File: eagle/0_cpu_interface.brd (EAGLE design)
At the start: 160 x 100 mm, 66 parts, among them IC1 74LS08N, IC10 74LS74N, IC11 74LS73N, IC12 MAX1232CPA, IC13 74LS32N, IC14 74LS244N, IC15 74LS74N, IC16 74LS14N, IC17 74LS541N, IC18 74LS541N, IC19 74LS541N, IC2 74LS541N, IC3 74LS245N, IC4 74LS245N, IC6 74LS541N, IC9 74LS74N

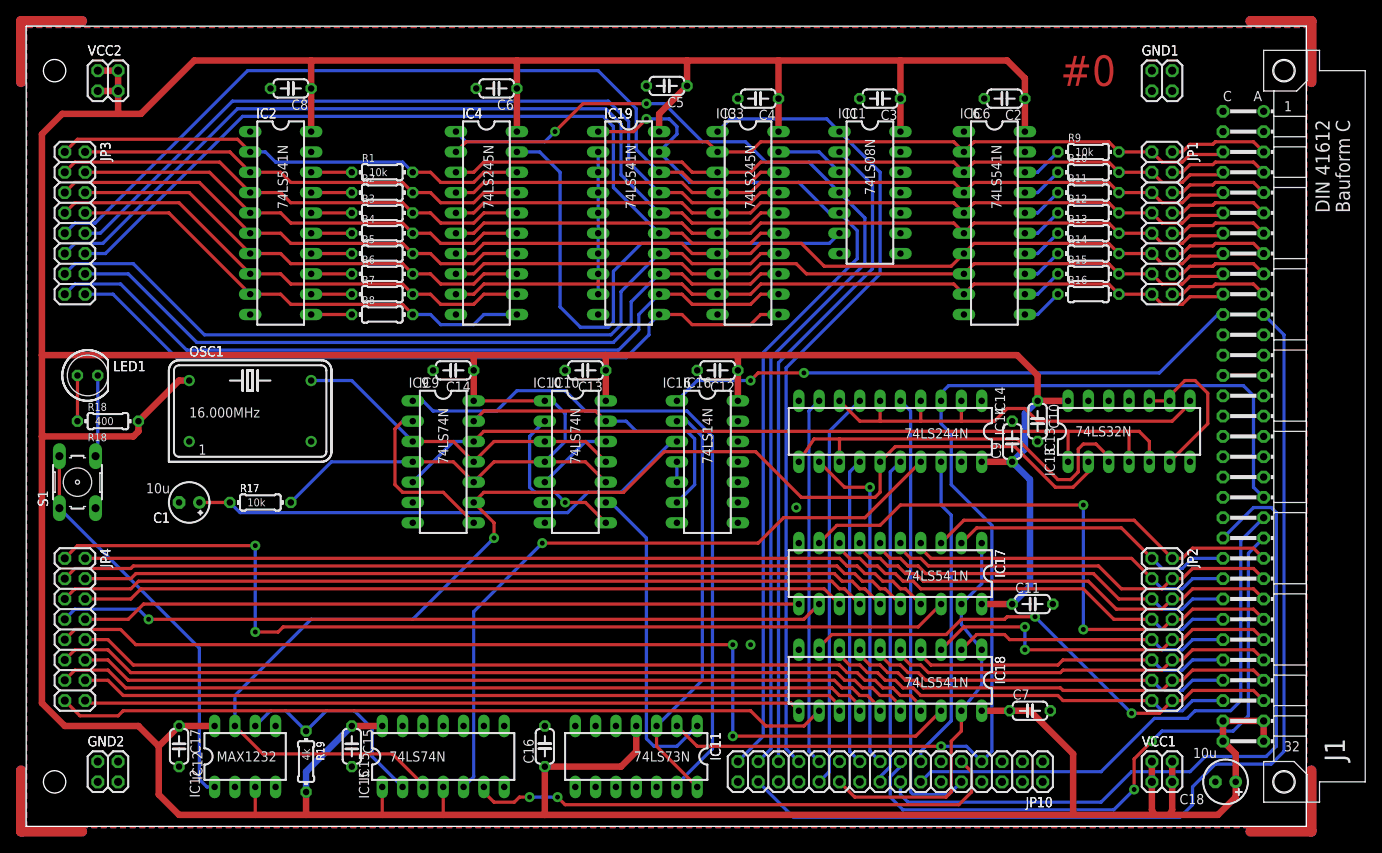
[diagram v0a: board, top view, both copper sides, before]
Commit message: All boards prepared for MMU extension
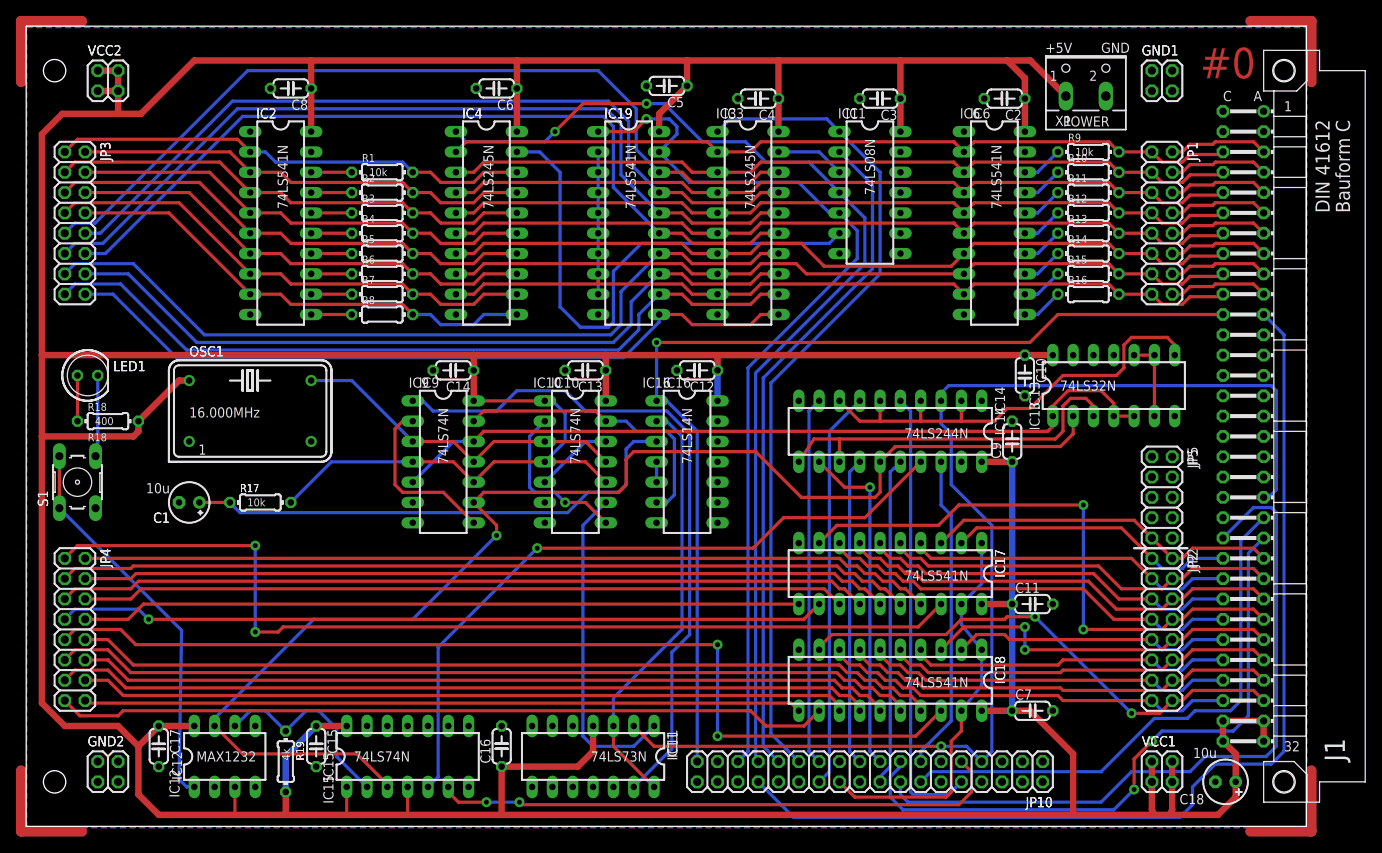
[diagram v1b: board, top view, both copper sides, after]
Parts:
- added JP5: (no value), pinhead:2X05
- added X1: (no value), con-wago-500:W237-102
- JP10: device pinhead:2X16 -> pinhead:2X18
- moved IC13 6.02 mm to (135.9, 55.2)
- moved C10 5.93 mm to (124.8, 56.5)
- moved IC11 5.40 mm to (70.8, 8.89)
- moved C16 5.40 mm to (59.4, 10.2)
- moved C15 4.45 mm to (36.2, 10.2)
- moved IC15 4.45 mm to (47.6, 8.89)
- moved C12 2.54 mm to (83.8, 57.1)
- moved IC16 2.54 mm to (82.5, 45.7)
- moved JP10 2.54 mm to (105.4, 6.99)
- moved C17 2.54 mm to (16.5, 10.2)
- moved IC12 2.54 mm to (24.8, 8.89)
- moved R19 2.54 mm to (32.4, 8.26)
- moved C7 0.32 mm to (125.7, 14.6)
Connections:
- new net /FP: JP10.34
- new net /NP_FAULT: JP10.36
- new net /WR_FAULT: JP10.33
- net +5V: now also X1.1
- net /IO: now also JP10.35
- net GND: now also X1.2
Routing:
- net /IO: track 72.7 -> 127.5 mm, vias 2 -> 1
- net N$29: track 19.9 -> 10.2 mm
- net /RST: track 142.3 -> 151.5 mm
- net CLK0: track 105.4 -> 98.6 mm
- net +5V: track 802.7 -> 807.5 mm
- net RST: track 67.8 -> 71.7 mm
- net N$26: track 55.0 -> 58.3 mm
- net BUSCLK: track 50.0 -> 46.8 mm
- net N$30: track 167.5 -> 165.4 mm
- net N$24: track 27.3 -> 25.4 mm
- net N$23: track 86.1 -> 87.9 mm
- net N$35: track 38.5 -> 36.7 mm
- net N$27: track 87.1 -> 85.4 mm
- net /MEM2ALUHI: track 82.8 -> 84.4 mm
- net /ALUHI2MEM: track 102.9 -> 104.5 mm
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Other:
- board text added: "+5V"
- board text added: "GND"
- board text added: "JP5"
- board text added: "POWER"

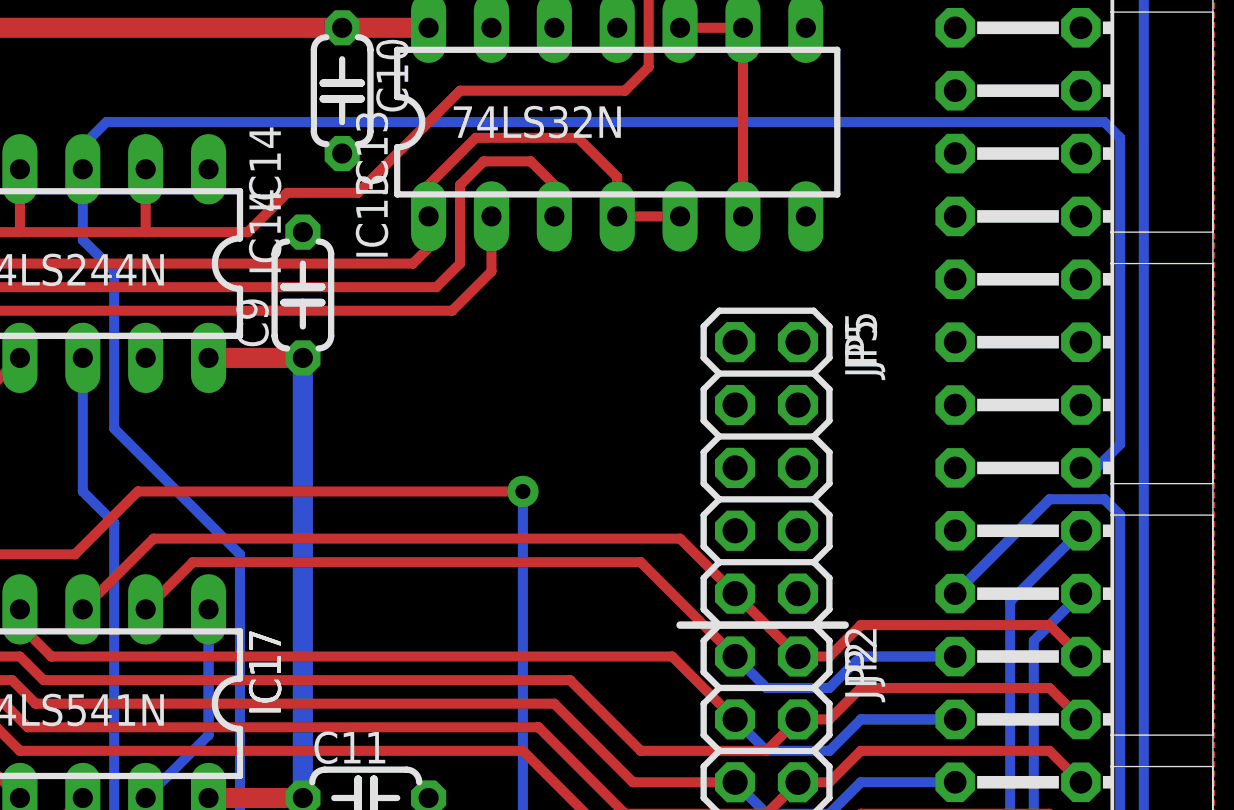
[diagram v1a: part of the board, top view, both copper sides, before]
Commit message: Parts library updated (added fast SRAM), MMU board half complete
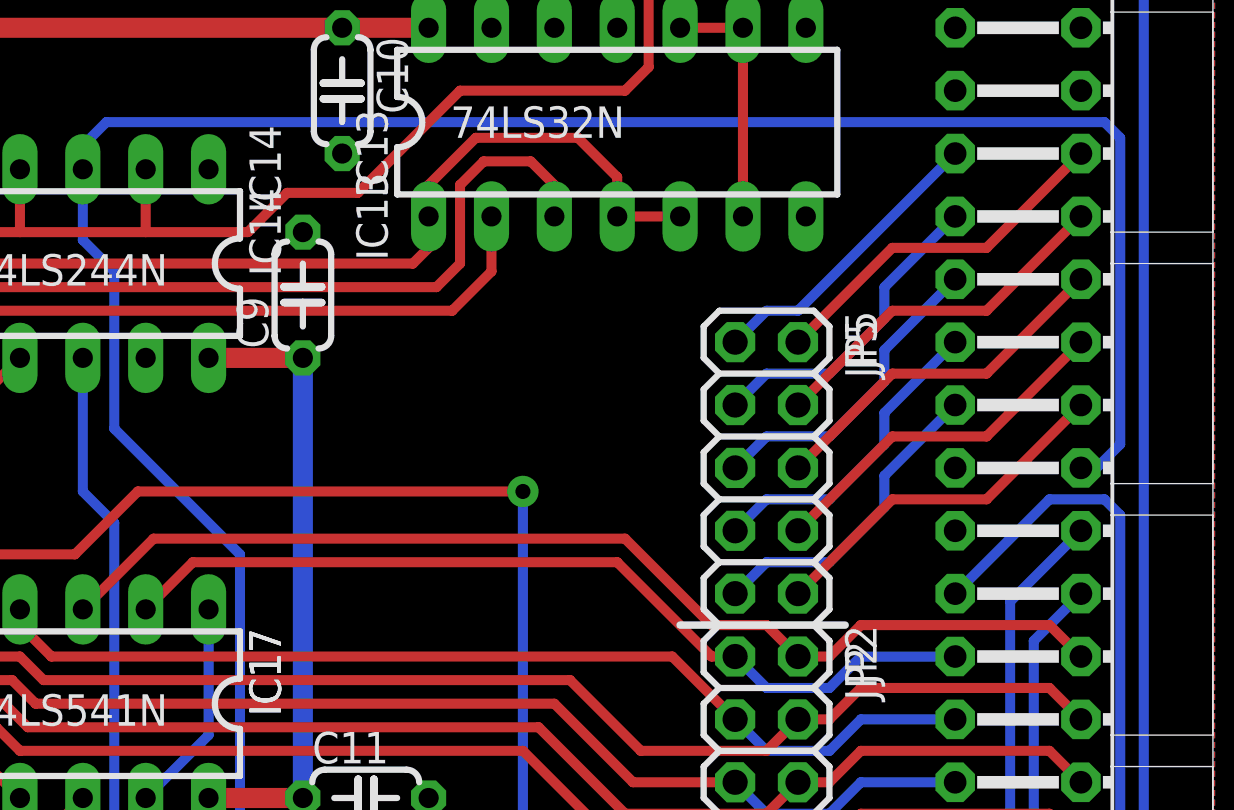
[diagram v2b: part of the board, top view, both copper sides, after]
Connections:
- new net PABUS12: J1.C15, JP5.1
- new net PABUS13: J1.A15, JP5.2
- new net PABUS14: J1.C16, JP5.3
- new net PABUS15: J1.A16, JP5.4
- new net PABUS16: J1.C17, JP5.5
- new net PABUS17: J1.A17, JP5.6
- new net PABUS18: J1.C18, JP5.7
- new net PABUS19: J1.A18, JP5.8
- new net PABUS20: J1.C19, JP5.9
- new net PABUS21: J1.A19, JP5.10
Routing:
- net PABUS17: track 0.00 -> 14.6 mm
- net PABUS15: track 0.00 -> 14.6 mm
- net PABUS13: track 0.00 -> 14.6 mm
- net PABUS21: track 0.00 -> 14.6 mm
- net PABUS19: track 0.00 -> 14.6 mm
- net PABUS16: track 0.00 -> 12.8 mm
- net PABUS14: track 0.00 -> 12.8 mm
- net PABUS20: track 0.00 -> 12.8 mm
- net PABUS18: track 0.00 -> 12.8 mm
- net PABUS12: track 0.00 -> 12.0 mm
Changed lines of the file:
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@@
 <wire x1="144.4625" y1="32.385" x2="141.9225" y2="32.385" width="0.4064" layer="16"/>
 <wire x1="141.9225" y1="32.385" x2="140.6525" y2="33.655" width="0.4064" layer="16"/>
-<wire x1="140.6525" y1="33.655" x2="136.8425" y2="37.465" width="0.4064" layer="1"/>
-<wire x1="136.8425" y1="37.465" x2="118.745" y2="37.465" width="0.4064" layer="1"/>
+<wire x1="135.89" y1="37.465" x2="118.745" y2="37.465" width="0.4064" layer="1"/>
 <wire x1="118.745" y1="37.465" x2="116.84" y2="35.56" width="0.4064" layer="1"/>
+<wire x1="140.6525" y1="33.655" x2="139.7" y2="33.655" width="0.4064" layer="1"/>
+<wire x1="139.7" y1="33.655" x2="135.89" y2="37.465" width="0.4064" layer="1"/>
 </signal>
 <signal name="ABUS1">
@@
 <wire x1="145.7325" y1="34.925" x2="144.4625" y2="33.655" width="0.4064" layer="1"/>
 <wire x1="144.4625" y1="33.655" x2="143.1925" y2="33.655" width="0.4064" layer="1"/>
-<wire x1="143.1925" y1="33.655" x2="138.43" y2="38.4175" width="0.4064" layer="1"/>
-<wire x1="138.43" y1="38.4175" x2="117.1575" y2="38.4175" width="0.4064" layer="1"/>
+<wire x1="136.2075" y1="38.4175" x2="117.1575" y2="38.4175" width="0.4064" layer="1"/>
 <wire x1="117.1575" y1="38.4175" x2="114.3" y2="35.56" width="0.4064" layer="1"/>
+<wire x1="143.1925" y1="33.655" x2="141.9225" y2="34.925" width="0.4064" layer="1"/>
+<wire x1="141.9225" y1="34.925" x2="139.7" y2="34.925" width="0.4064" layer="1"/>
+<wire x1="139.7" y1="34.925" x2="136.2075" y2="38.4175" width="0.4064" layer="1"/>
 </signal>
 <signal name="ABUS2">
@@
 <contactref element="JP10" pad="36"/>
 </signal>
+<signal name="PABUS12">
+<contactref element="JP5" pad="1"/>
+<contactref element="J1" pad="C15"/>
+<wire x1="140.6525" y1="46.355" x2="141.9225" y2="47.625" width="0.4064" layer="16"/>
+<wire x1="141.9225" y1="47.625" x2="143.1925" y2="47.625" width="0.4064" layer="16"/>
+<wire x1="143.1925" y1="47.625" x2="149.5425" y2="53.975" width="0.4064" layer="16"/>
+</signal>
+<signal name="PABUS13">
+<contactref element="JP5" pad="2"/>
+<contactref element="J1" pad="A15"/>
+<wire x1="143.1925" y1="46.355" x2="147.0025" y2="50.165" width="0.4064" layer="1"/>
+<wire x1="147.0025" y1="50.165" x2="150.8125" y2="50.165" width="0.4064" layer="1"/>
+<wire x1="150.8125" y1="50.165" x2="154.6225" y2="53.975" width="0.4064" layer="1"/>
+</signal>
+<signal name="PABUS14">
+<contactref element="JP5" pad="3"/>
+<contactref element="J1" pad="C16"/>
+<wire x1="140.6525" y1="43.815" x2="141.9225" y2="45.085" width="0.4064" layer="16"/>
+<wire x1="141.9225" y1="45.085" x2="144.4625" y2="45.085" width="0.4064" layer="16"/>
+<wire x1="144.4625" y1="45.085" x2="146.685" y2="47.3075" width="0.4064" layer="16"/>
+<wire x1="146.685" y1="47.3075" x2="146.685" y2="48.5775" width="0.4064" layer="16"/>
+<wire x1="146.685" y1="48.5775" x2="149.5425" y2="51.435" width="0.4064" layer="16"/>
+</signal>
+<signal name="PABUS15">
+<contactref element="JP5" pad="4"/>
+<contactref element="J1" pad="A16"/>
+<wire x1="143.1925" y1="43.815" x2="147.0025" y2="47.625" width="0.4064" layer="1"/>
+<wire x1="147.0025" y1="47.625" x2="150.8125" y2="47.625" width="0.4064" layer="1"/>
+<wire x1="150.8125" y1="47.625" x2="154.6225" y2="51.435" width="0.4064" layer="1"/>
+</signal>
+<signal name="PABUS16">
+<contactref element="J1" pad="C17"/>
+<contactref element="JP5" pad="5"/>
+<wire x1="140.6525" y1="41.275" x2="141.9225" y2="42.545" width="0.4064" layer="16"/>
+<wire x1="141.9225" y1="42.545" x2="144.4625" y2="42.545" width="0.4064" layer="16"/>
+<wire x1="144.4625" y1="42.545" x2="146.685" y2="44.7675" width="0.4064" layer="16"/>
+<wire x1="146.685" y1="44.7675" x2="146.685" y2="46.0375" width="0.4064" layer="16"/>
+<wire x1="146.685" y1="46.0375" x2="149.5425" y2="48.895" width="0.4064" layer="16"/>
+</signal>
+<signal name="PABUS18">
+<contactref element="J1" pad="C18"/>
+<contactref element="JP5" pad="7"/>
+<wire x1="140.6525" y1="38.735" x2="141.9225" y2="40.005" width="0.4064" layer="16"/>
+<wire x1="141.9225" y1="40.005" x2="144.4625" y2="40.005" width="0.4064" layer="16"/>
+<wire x1="144.4625" y1="40.005" x2="146.685" y2="42.2275" width="0.4064" layer="16"/>
+<wire x1="146.685" y1="42.2275" x2="146.685" y2="43.4975" width="0.4064" layer="16"/>
+<wire x1="146.685" y1="43.4975" x2="149.5425" y2="46.355" width="0.4064" layer="16"/>
+</signal>
+<signal name="PABUS20">
+<contactref element="J1" pad="C19"/>
+<contactref element="JP5" pad="9"/>
+<wire x1="140.6525" y1="36.195" x2="141.9225" y2="37.465" width="0.4064" layer="16"/>
+<wire x1="141.9225" y1="37.465" x2="144.4625" y2="37.465" width="0.4064" layer="16"/>
+<wire x1="144.4625" y1="37.465" x2="146.685" y2="39.6875" width="0.4064" layer="16"/>
+<wire x1="146.685" y1="39.6875" x2="146.685" y2="40.9575" width="0.4064" layer="16"/>
+<wire x1="146.685" y1="40.9575" x2="149.5425" y2="43.815" width="0.4064" layer="16"/>
+</signal>
+<signal name="PABUS17">
+<contactref element="J1" pad="A17"/>
+<contactref element="JP5" pad="6"/>
+<wire x1="143.1925" y1="41.275" x2="147.0025" y2="45.085" width="0.4064" layer="1"/>
+<wire x1="147.0025" y1="45.085" x2="150.8125" y2="45.085" width="0.4064" layer="1"/>
+<wire x1="150.8125" y1="45.085" x2="154.6225" y2="48.895" width="0.4064" layer="1"/>
+</signal>
+<signal name="PABUS19">
+<contactref element="J1" pad="A18"/>
+<contactref element="JP5" pad="8"/>
+<wire x1="143.1925" y1="38.735" x2="147.0025" y2="42.545" width="0.4064" layer="1"/>
+<wire x1="147.0025" y1="42.545" x2="150.8125" y2="42.545" width="0.4064" layer="1"/>
+<wire x1="150.8125" y1="42.545" x2="154.6225" y2="46.355" width="0.4064" layer="1"/>
+</signal>
+<signal name="PABUS21">
+<contactref element="J1" pad="A19"/>
+<contactref element="JP5" pad="10"/>
+<wire x1="143.1925" y1="36.195" x2="147.0025" y2="40.005" width="0.4064" layer="1"/>
+<wire x1="147.0025" y1="40.005" x2="150.8125" y2="40.005" width="0.4064" layer="1"/>
+<wire x1="150.8125" y1="40.005" x2="154.6225" y2="43.815" width="0.4064" layer="1"/>
+</signal>
 </signals>

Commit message: MMU schematics update
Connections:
- new net /ENMEMX: J1.C22
- new net /LDMEMX: J1.A22
- net /ENMEM: no longer J1.C22
- net /LDMEM: no longer J1.A22
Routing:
- net /ENMEM: track 89.6 -> 84.2 mm
- net /LDMEM: track 80.5 -> 77.8 mm
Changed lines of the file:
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@@
 </signal>
 <signal name="/ENMEM">
-<contactref element="J1" pad="C22"/>
 <wire x1="109.22" y1="4.1275" x2="110.1725" y2="3.175" width="0.4064" layer="16"/>
 <wire x1="110.1725" y1="3.175" x2="134.3025" y2="3.175" width="0.4064" layer="16"/>
@@
 <wire x1="156.21" y1="39.37" x2="155.575" y2="40.005" width="0.4064" layer="16"/>
 <wire x1="155.575" y1="40.005" x2="153.3525" y2="40.005" width="0.4064" layer="16"/>
-<wire x1="153.3525" y1="40.005" x2="149.5425" y2="36.195" width="0.4064" layer="16"/>
 <wire x1="145.415" y1="6.985" x2="138.1125" y2="6.985" width="0.4064" layer="16"/>
 <wire x1="138.1125" y1="6.985" x2="134.3025" y2="3.175" width="0.4064" layer="16"/>
@@
 </signal>
 <signal name="/LDMEM">
-<contactref element="J1" pad="A22"/>
-<wire x1="154.6225" y1="36.195" x2="152.7175" y2="34.29" width="0.4064" layer="16"/>
 <wire x1="152.7175" y1="34.29" x2="152.7175" y2="13.97" width="0.4064" layer="16"/>
 <wire x1="152.7175" y1="13.97" x2="150.8125" y2="12.065" width="0.4064" layer="16"/>
@@
 <wire x1="150.8125" y1="40.005" x2="154.6225" y2="43.815" width="0.4064" layer="1"/>
 </signal>
+<signal name="/LDMEMX">
+<contactref element="J1" pad="A22"/>
+</signal>
+<signal name="/ENMEMX">
+<contactref element="J1" pad="C22"/>
+</signal>
 </signals>

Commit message: More MMU changes, added PPREG
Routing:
- net /ENMEM: track 84.2 -> 0.00 mm
- net /LDMEM: track 77.8 -> 0.00 mm, vias 2 -> 0
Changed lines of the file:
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@@
 </signal>
 <signal name="/ENMEM">
-<wire x1="109.22" y1="4.1275" x2="110.1725" y2="3.175" width="0.4064" layer="16"/>
-<wire x1="110.1725" y1="3.175" x2="134.3025" y2="3.175" width="0.4064" layer="16"/>
-<wire x1="156.21" y1="10.16" x2="156.21" y2="39.37" width="0.4064" layer="16"/>
-<wire x1="156.21" y1="39.37" x2="155.575" y2="40.005" width="0.4064" layer="16"/>
-<wire x1="155.575" y1="40.005" x2="153.3525" y2="40.005" width="0.4064" layer="16"/>
-<wire x1="145.415" y1="6.985" x2="138.1125" y2="6.985" width="0.4064" layer="16"/>
-<wire x1="138.1125" y1="6.985" x2="134.3025" y2="3.175" width="0.4064" layer="16"/>
-<wire x1="145.415" y1="6.985" x2="147.32" y2="8.89" width="0.4064" layer="16"/>
-<wire x1="147.32" y1="8.89" x2="154.94" y2="8.89" width="0.4064" layer="16"/>
-<wire x1="154.94" y1="8.89" x2="156.21" y2="10.16" width="0.4064" layer="16"/>
 <contactref element="JP10" pad="16"/>
-<wire x1="109.22" y1="5.715" x2="109.22" y2="4.1275" width="0.4064" layer="16"/>
 </signal>
 <signal name="/LDMEM">
-<wire x1="152.7175" y1="34.29" x2="152.7175" y2="13.97" width="0.4064" layer="16"/>
-<wire x1="152.7175" y1="13.97" x2="150.8125" y2="12.065" width="0.4064" layer="16"/>
-<wire x1="140.6525" y1="10.795" x2="138.43" y2="8.5725" width="0.4064" layer="1"/>
-<wire x1="138.43" y1="8.5725" x2="138.43" y2="4.7625" width="0.4064" layer="1"/>
-<wire x1="138.43" y1="4.7625" x2="135.89" y2="2.2225" width="0.4064" layer="16"/>
-<wire x1="135.89" y1="2.2225" x2="109.5375" y2="2.2225" width="0.4064" layer="16"/>
-<wire x1="109.5375" y1="2.2225" x2="107.95" y2="3.81" width="0.4064" layer="16"/>
-<wire x1="107.95" y1="3.81" x2="107.95" y2="6.35" width="0.4064" layer="16"/>
-<via x="140.6525" y="10.795" extent="1-16" drill="0.6096" diameter="1.27"/>
-<via x="138.43" y="4.7625" extent="1-16" drill="0.6096" diameter="1.27"/>
-<wire x1="107.95" y1="6.35" x2="109.22" y2="7.62" width="0.4064" layer="16"/>
 <contactref element="JP10" pad="15"/>
-<wire x1="109.22" y1="8.255" x2="109.22" y2="7.62" width="0.4064" layer="16"/>
-<wire x1="140.6525" y1="10.795" x2="141.9225" y2="12.065" width="0.4064" layer="16"/>
-<wire x1="141.9225" y1="12.065" x2="150.8125" y2="12.065" width="0.4064" layer="16"/>
 </signal>
 <signal name="MEMSEG">

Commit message: Removal of PPC started
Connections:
- removed net /LDPPC: JP10.11
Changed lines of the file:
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@@
 <contactref element="JP10" pad="1"/>
-</signal>
-<signal name="/LDPPC">
-<contactref element="JP10" pad="11"/>
 </signal>
 <signal name="PROT">

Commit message: Completed board 0
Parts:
- JP5: device pinhead:2X05 -> pinhead:2X06
- moved IC13 1.91 mm to (135.9, 57.1)
- moved JP5 1.27 mm to (141.9, 42.5)
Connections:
- new net /MEMOP: JP10.11
- net /ENMEMX: now also JP5.11
- net /FS: no longer J1.A11
- net /LDMEMX: now also JP5.12
- net MEMSEG: no longer J1.A21
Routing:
- net /FS: track 127.9 -> 0.00 mm
- net MEMSEG: track 68.3 -> 0.00 mm
- net /LDMEMX: track 0.00 -> 12.5 mm
- net /ENMEMX: track 0.00 -> 9.94 mm
- net BUSCLK: track 46.8 -> 49.1 mm
- net CLK0: track 98.6 -> 100.7 mm
- net N$30: track 165.4 -> 167.3 mm
- net PABUS20: track 12.8 -> 11.0 mm
- net PABUS18: track 12.8 -> 11.0 mm
- net PABUS16: track 12.8 -> 11.0 mm
- net PABUS14: track 12.8 -> 11.0 mm
- net N$26: track 58.3 -> 60.0 mm
- net PABUS13: track 14.6 -> 13.5 mm
- net PABUS12: track 12.0 -> 11.0 mm
- net PABUS21: track 14.6 -> 13.5 mm
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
